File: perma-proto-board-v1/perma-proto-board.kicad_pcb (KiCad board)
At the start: 2 copper layers, 156.2 x 81.3 mm, 50 parts, among them J1 SPI_01, J10 I2C_04, J11 I2C_05, J12 I2C_06, J13 A_1, J14 A_2, J15 A_3, J16 A_4, J17 A_5, J18 B_1, J19 B_2, J2 SPI_02, J20 B_3, J21 B_4, J22 B_5, J23 C_1, J24 C_2, J25 C_3, J26 C_4, J27 C_5, J28 Power01, J29 Power02, J3 SPI_03, J30 Power03, J31 Power04, J32 Rail01, J33 Rail02, J36 Rail05, J37 Rail06, J4 SPI_04, J40 USB_C_Receptacle, J41 SPI_CS_01, J42 SPI_CS_02, J43 SPI_CS_03, J44 SPI_CS_04, J45 SPI_CS_05, J46 SPI_CS_06, J5 SPI_05, J6 SPI_06, J7 I2C_01, J8 I2C_02, J9 I2C_03

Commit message: v1.1
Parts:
- J13, J14, J15, J16, J17, J18, J19, J20, J21, J22, J23, J24, J25, J26, J27, J32, J33, J36, J37: footprint Connector_PinHeader_2.54mm:PinHeader_1x40_P2.54mm_Vertical -> perma-proto-board-v1:PinHeader_1x40_P2.54mm_Vertical_NO_Silk
- J34, J38: renamed from -; footprint Connector_PinHeader_2.54mm:PinHeader_1x40_P2.54mm_Vertical -> perma-proto-board-v1:PinHeader_1x40_P2.54mm_Vertical_NO_Silk
- J35, J39: renamed from +; footprint Connector_PinHeader_2.54mm:PinHeader_1x40_P2.54mm_Vertical -> perma-proto-board-v1:PinHeader_1x40_P2.54mm_Vertical_NO_Silk
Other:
- board text added: "113.03->"
- board text added: "<- 45.72 ->"
- board text added: "https://github.com/citizen-science-and-engineering/perma-proto-board v1.1"
- board text removed: "https://github.com/citizen-science-and-engineering/perma-proto-board"

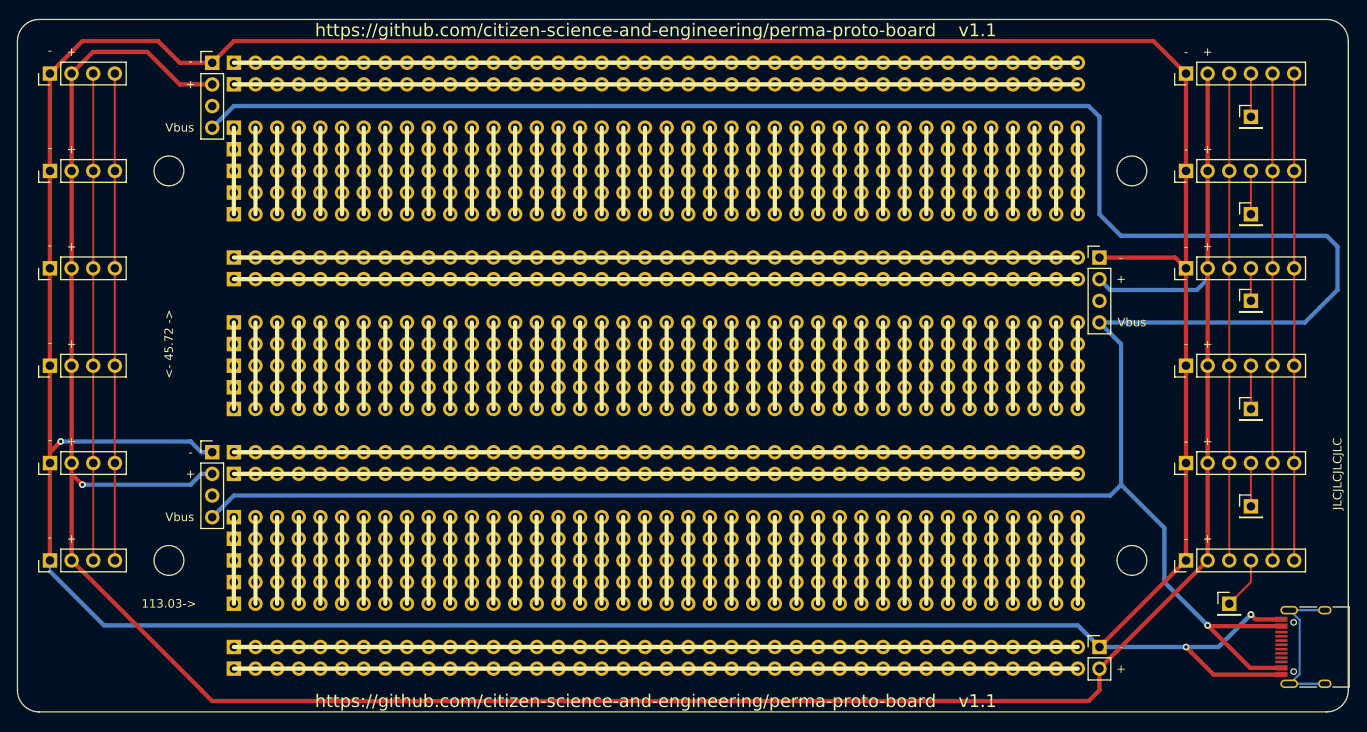
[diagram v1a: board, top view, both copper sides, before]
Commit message: silk screen fix
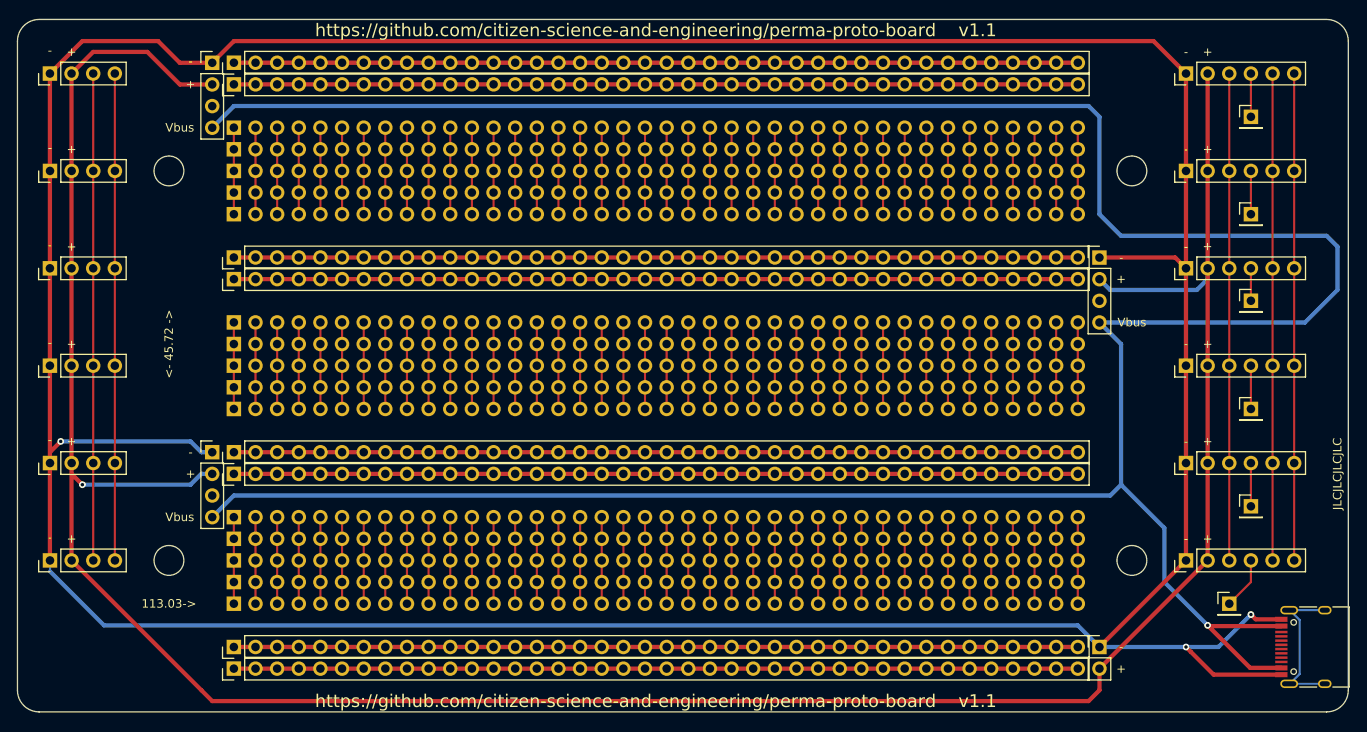
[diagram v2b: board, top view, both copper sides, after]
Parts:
- J32, J33, J34, J35, J36, J37, J38, J39: footprint perma-proto-board-v1:PinHeader_1x40_P2.54mm_Vertical_NO_Silk -> Connector_PinHeader_2.54mm:PinHeader_1x40_P2.54mm_Vertical
